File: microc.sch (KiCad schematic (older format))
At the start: 17 parts, among them J1 Conn_01x12, J2 Conn_01x12, J3 USB_C_Receptacle_USB2.0, U2 USBLC6-2SC6, U3 ATmega32U4RC-AU, Y1 16mhz

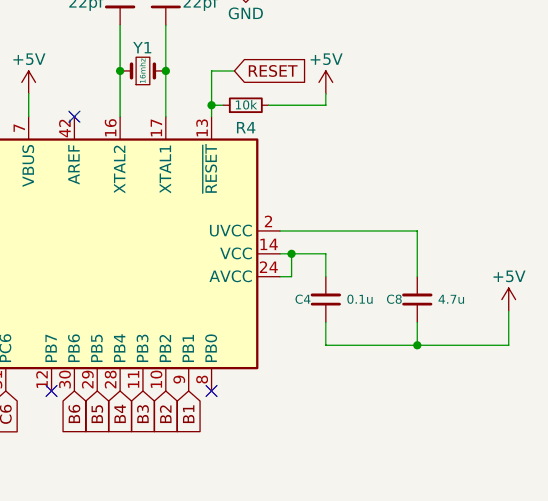
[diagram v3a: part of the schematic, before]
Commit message: rev 1.3 - Improved ground plane - Updated routing - Fixed error with power in schematic
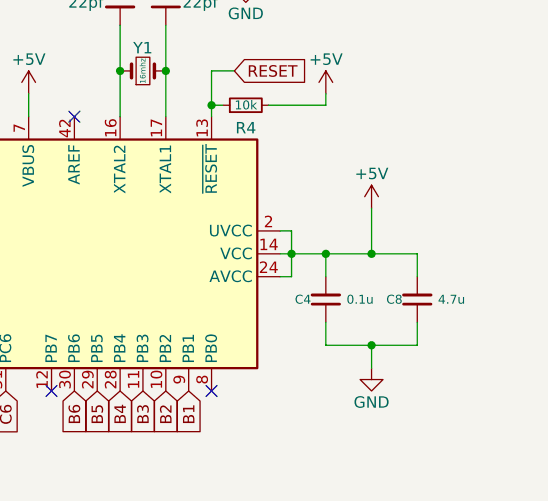
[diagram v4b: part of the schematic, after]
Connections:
- net +5V: now also C4.2, C8.2, U3.14 (VCC), U3.2 (UVCC), U3.24 (AVCC), U3.34 (VCC), U3.44 (AVCC); no longer C4.1, C8.1
- net GND: now also C4.1, C8.1
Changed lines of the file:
@@
 Wire Wire Line
 	8400 4800 8400 4700
-Connection ~ 8800 5100
 Wire Wire Line
 	8800 5000 8800 5100
 Wire Wire Line
-	8400 5100 8800 5100
+	8400 5100 8600 5100
 Wire Wire Line
 	8400 5000 8400 5100
@@
 	8200 4700 8250 4700
 Connection ~ 8250 4700
-Wire Wire Line
-	8200 4600 8800 4600
 Connection ~ 4750 3700
 $Comp
@@
 L power:+5V #PWR0106
 U 1 1 6142AA7E
-P 9200 4950
-F 0 "#PWR0106" H 9200 4800 50  0001 C CNN
-F 1 "+5V" H 9200 5100 50  0000 C CNN
-F 2 "" H 9200 4950 50  0001 C CNN
-F 3 "" H 9200 4950 50  0001 C CNN
-	1    9200 4950
-	1    0    0    -1
-$EndComp
-Wire Wire Line
-	9200 5100 9200 4950
-Wire Wire Line
-	8800 5100 9200 5100
-Wire Wire Line
-	8800 4800 8800 4600
+P 8600 4500
+F 0 "#PWR0106" H 8600 4350 50  0001 C CNN
+F 1 "+5V" H 8600 4650 50  0000 C CNN
+F 2 "" H 8600 4500 50  0001 C CNN
+F 3 "" H 8600 4500 50  0001 C CNN
+	1    8600 4500
+	1    0    0    -1
+$EndComp
 $Comp
 L MCU_Microchip_ATmega:ATmega32U4RC-AU U3
@@
 Wire Wire Line
 	5350 2700 5900 2700
+Wire Wire Line
+	8200 4600 8250 4600
+Wire Wire Line
+	8250 4600 8250 4700
+Wire Wire Line
+	8400 4700 8600 4700
+Wire Wire Line
+	8800 4700 8800 4800
+Connection ~ 8400 4700
+$Comp
+L power:GND #PWR0116
+U 1 1 6101E8C4
+P 8600 5200
+F 0 "#PWR0116" H 8600 4950 50  0001 C CNN
+F 1 "GND" H 8600 5050 50  0000 C CNN
+F 2 "" H 8600 5200 50  0001 C CNN
+F 3 "" H 8600 5200 50  0001 C CNN
+	1    8600 5200
+	1    0    0    -1
+$EndComp
+Wire Wire Line
+	8600 5200 8600 5100
+Connection ~ 8600 5100
+Wire Wire Line
+	8600 5100 8800 5100
+Wire Wire Line
+	8600 4500 8600 4700
+Connection ~ 8600 4700
+Wire Wire Line
+	8600 4700 8800 4700
 $EndSCHEMATC

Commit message: r
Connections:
- net +5V: no longer R1.1, R2.1
- net GND: now also R1.1, R2.1
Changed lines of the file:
@@
 	0    1    1    0
-$EndComp
-$Comp
-L power:+5V #PWR0102
-U 1 1 61023575
-P 5750 2200
-F 0 "#PWR0102" H 5750 2050 50  0001 C CNN
-F 1 "+5V" H 5750 2350 50  0000 C CNN
-F 2 "" H 5750 2200 50  0001 C CNN
-F 3 "" H 5750 2200 50  0001 C CNN
-	1    5750 2200
-	1    0    0    -1
 $EndComp
 Wire Wire Line
@@
 Wire Wire Line
 	5650 2300 5750 2300
-Connection ~ 5750 2300
-Wire Wire Line
-	5750 2300 5750 2200
 Wire Wire Line
 	5350 2800 5450 2800
@@
 Wire Wire Line
 	8600 4700 8800 4700
+$Comp
+L power:GND #PWR?
+U 1 1 611BAFE0
+P 5750 2400
+F 0 "#PWR?" H 5750 2150 50  0001 C CNN
+F 1 "GND" H 5750 2250 50  0000 C CNN
+F 2 "" H 5750 2400 50  0001 C CNN
+F 3 "" H 5750 2400 50  0001 C CNN
+	1    5750 2400
+	1    0    0    -1
+$EndComp
+Connection ~ 5750 2400
 $EndSCHEMATC
